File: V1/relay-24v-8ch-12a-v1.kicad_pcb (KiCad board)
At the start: 2 copper layers, 98 x 67.8 mm, 44 parts, among them J1 DB141V-2.54-6P, J2 DB141V-2.54-6P, J3 DB142V-5.08-8P, J4 DB142V-5.08-8P, K1 G5PZ-1A, K2 G5PZ-1A, K3 G5PZ-1A, K4 G5PZ-1A, K5 G5PZ-1A, K6 G5PZ-1A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

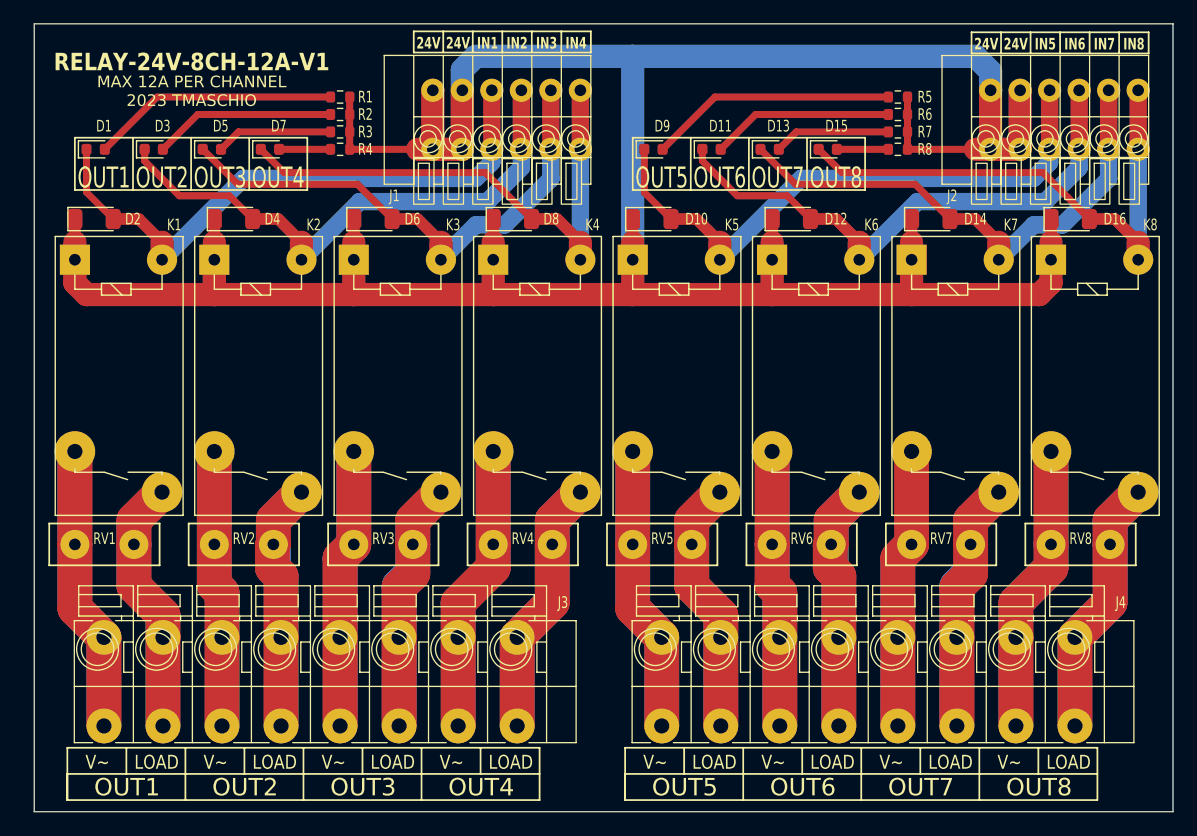
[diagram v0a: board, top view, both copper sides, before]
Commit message: Updated connectors
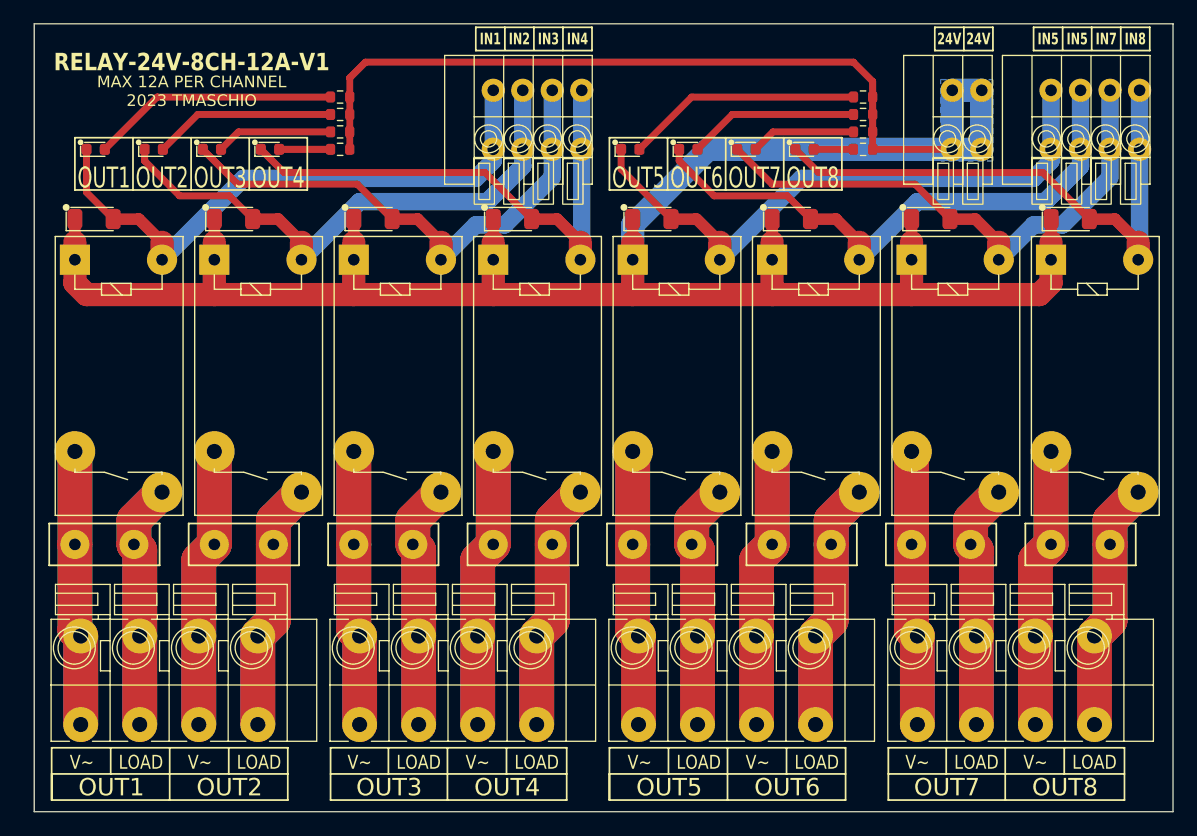
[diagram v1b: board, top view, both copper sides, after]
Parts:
- added J5: DB142V-5.08-4P, Tales:TerminalBlock_Dibo_DB142V-5.08-4P_1x04_P5.08mm_Vertical, F.Cu at (153.0, 122.5)
- added J6: DB142V-5.08-4P, Tales:TerminalBlock_Dibo_DB142V-5.08-4P_1x04_P5.08mm_Vertical, F.Cu at (177.0, 122.5)
- added J7: DB142V-5.08-4P, Tales:TerminalBlock_Dibo_DB142V-5.08-4P_1x04_P5.08mm_Vertical, F.Cu at (201.0, 122.5)
- J1: value DB141V-2.54-6P -> DB141V-2.54-2P; footprint Tales:TerminalBlock_Dibo_DB141V-2.54-6P_1x06_P2.54mm_Vertical -> Tales:TerminalBlock_Dibo_DB141V-2.54-2P_1x02_P2.54mm_Vertical
- J2: value DB141V-2.54-6P -> DB141V-2.54-4P; footprint Tales:TerminalBlock_Dibo_DB141V-2.54-6P_1x06_P2.54mm_Vertical -> Tales:TerminalBlock_Dibo_DB141V-2.54-4P_1x04_P2.54mm_Vertical
- J3: value DB142V-5.08-8P -> DB141V-2.54-4P; footprint Tales:TerminalBlock_Dibo_DB142V-5.08-8P_1x08_P5.08mm_Vertical -> Tales:TerminalBlock_Dibo_DB141V-2.54-4P_1x04_P2.54mm_Vertical
- J4: value DB142V-5.08-8P -> DB142V-5.08-4P; footprint Tales:TerminalBlock_Dibo_DB142V-5.08-8P_1x08_P5.08mm_Vertical -> Tales:TerminalBlock_Dibo_DB142V-5.08-4P_1x04_P5.08mm_Vertical
- R1, R2, R3, R4, R5, R6, R7, R8: value 5k6/100mW -> 6k8/100mW
- moved J3 104.6 mm to (220.1, 67.9), turned to 180 degrees
- moved J4 50.0 mm to (129.0, 122.5)
- moved J2 47.9 mm to (172.1, 67.9)
- moved J1 34.5 mm to (206.5, 67.9)
- moved R5 3.00 mm to (196.3, 68.5)
- moved R6 3.00 mm to (196.3, 70.0)
- moved R7 3.00 mm to (196.3, 71.5)
- moved R8 3.00 mm to (196.3, 73.0)
- moved D11 2.00 mm to (181.3, 73.0)
- moved D13 2.00 mm to (186.3, 73.0)
- moved D15 2.00 mm to (191.3, 73.0)
- moved D9 2.00 mm to (176.3, 73.0)
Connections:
- J1 pad 1: Net-(D7-K) -> +24V
- J1 pad 2: Net-(D5-K) -> +24V
- J2 pad 1: Net-(D15-K) -> Net-(D7-K)
- J2 pad 2: Net-(D13-K) -> Net-(D5-K)
- J2 pad 3: Net-(D11-K) -> Net-(D3-K)
- J2 pad 4: Net-(D10-A) -> Net-(D1-K)
- J3 pad 1: Net-(J3-Pin_1) -> Net-(D15-K)
- J3 pad 2: Net-(J3-Pin_2) -> Net-(D13-K)
- J3 pad 3: Net-(J3-Pin_3) -> Net-(D11-K)
- J3 pad 4: Net-(J3-Pin_4) -> Net-(D10-A)
- K1 pad 2: Net-(J3-Pin_1) -> Net-(J4-Pin_1)
- K1 pad 3: Net-(J3-Pin_2) -> Net-(J4-Pin_2)
- K2 pad 2: Net-(J3-Pin_3) -> Net-(J4-Pin_3)
- K2 pad 3: Net-(J3-Pin_4) -> Net-(J4-Pin_4)
- K3 pad 2: Net-(J3-Pin_5) -> Net-(J5-Pin_1)
- K3 pad 3: Net-(J3-Pin_6) -> Net-(J5-Pin_2)
- K4 pad 2: Net-(J3-Pin_7) -> Net-(J5-Pin_3)
- K4 pad 3: Net-(J3-Pin_8) -> Net-(J5-Pin_4)
- K5 pad 2: Net-(J4-Pin_1) -> Net-(J6-Pin_1)
- K5 pad 3: Net-(J4-Pin_2) -> Net-(J6-Pin_2)
- K6 pad 2: Net-(J4-Pin_3) -> Net-(J6-Pin_3)
- K6 pad 3: Net-(J4-Pin_4) -> Net-(J6-Pin_4)
- K7 pad 2: Net-(J4-Pin_5) -> Net-(J7-Pin_1)
- K7 pad 3: Net-(J4-Pin_6) -> Net-(J7-Pin_2)
- K8 pad 2: Net-(J4-Pin_7) -> Net-(J7-Pin_3)
- K8 pad 3: Net-(J4-Pin_8) -> Net-(J7-Pin_4)
- RV1 pad 1: Net-(J3-Pin_1) -> Net-(J4-Pin_1)
- RV1 pad 2: Net-(J3-Pin_2) -> Net-(J4-Pin_2)
- RV2 pad 1: Net-(J3-Pin_3) -> Net-(J4-Pin_3)
- RV2 pad 2: Net-(J3-Pin_4) -> Net-(J4-Pin_4)
- RV3 pad 1: Net-(J3-Pin_5) -> Net-(J5-Pin_1)
- RV3 pad 2: Net-(J3-Pin_6) -> Net-(J5-Pin_2)
- RV4 pad 1: Net-(J3-Pin_7) -> Net-(J5-Pin_3)
- RV4 pad 2: Net-(J3-Pin_8) -> Net-(J5-Pin_4)
- RV5 pad 1: Net-(J4-Pin_1) -> Net-(J6-Pin_1)
- RV5 pad 2: Net-(J4-Pin_2) -> Net-(J6-Pin_2)
- RV6 pad 1: Net-(J4-Pin_3) -> Net-(J6-Pin_3)
- RV6 pad 2: Net-(J4-Pin_4) -> Net-(J6-Pin_4)
- RV7 pad 1: Net-(J4-Pin_5) -> Net-(J7-Pin_1)
- RV7 pad 2: Net-(J4-Pin_6) -> Net-(J7-Pin_2)
- RV8 pad 1: Net-(J4-Pin_7) -> Net-(J7-Pin_3)
- RV8 pad 2: Net-(J4-Pin_8) -> Net-(J7-Pin_4)
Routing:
- net Net-(J4-Pin_7): track 49.7 -> 0.00 mm
- net Net-(J3-Pin_7): track 49.7 -> 0.00 mm
- net Net-(J3-Pin_1): track 49.3 -> 0.00 mm
- net Net-(J4-Pin_5): track 48.2 -> 0.00 mm
- net Net-(J3-Pin_5): track 48.2 -> 0.00 mm
- net Net-(J7-Pin_3): track 0.00 -> 48.1 mm
- net Net-(J6-Pin_3): track 0.00 -> 48.1 mm
- net Net-(J5-Pin_3): track 0.00 -> 48.1 mm
- net Net-(J3-Pin_3): track 47.8 -> 0.00 mm
- net Net-(J7-Pin_1): track 0.00 -> 47.4 mm
- net Net-(J6-Pin_1): track 0.00 -> 47.4 mm
- net Net-(J5-Pin_1): track 0.00 -> 47.4 mm
- net Net-(J4-Pin_8): track 44.7 -> 0.00 mm
- net Net-(J3-Pin_8): track 44.7 -> 0.00 mm
- net Net-(J3-Pin_2): track 44.3 -> 0.00 mm
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- added copper zone on B.Cu, net +24V
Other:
- board text removed: "IN6"
